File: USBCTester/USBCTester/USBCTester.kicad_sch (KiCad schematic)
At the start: 63 parts, among them J1 AUSB1-DFN-PTR3, J2 AUSB1-DFN-PTR3, J4 Conn_01x03, J5 Conn_01x08, J6 Conn_01x03, SW1 SW_Push, U1 74HC595, U2 74HC595, U3 74HC595, U4 74HC595, U5 74HC595, U6 74HC595, U7 RaspberryPi_Pico

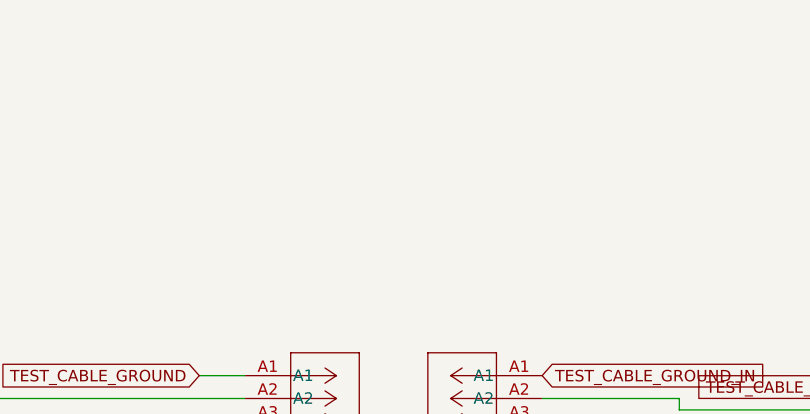
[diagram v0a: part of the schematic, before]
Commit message: add power plane and vias for high current and decoupling caps
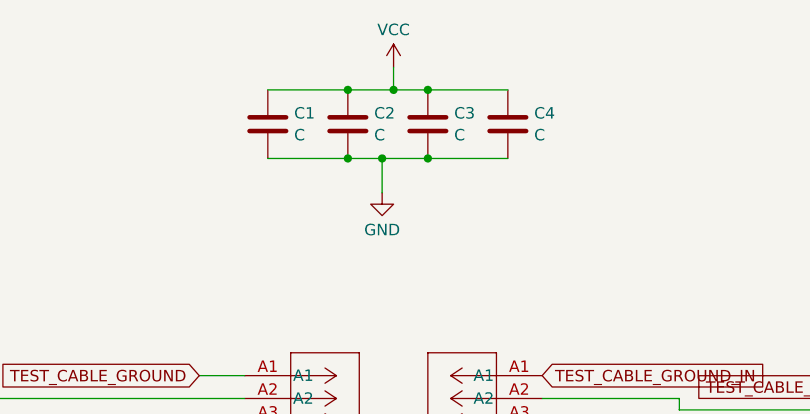
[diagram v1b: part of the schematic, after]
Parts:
- added C1, C2, C3, C4: C, symbol Device:C
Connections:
- net GND: now also C1.2, C2.2, C3.2, C4.2
- net VCC: now also C1.1, C2.1, C3.1, C4.1
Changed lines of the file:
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@@
   (junction (at 215.9 29.21) (diameter 0) (color 0 0 0 0)
   )
+  (junction (at 113.03 22.86) (diameter 0) (color 0 0 0 0)
+  )
   (junction (at 279.4 50.8) (diameter 0) (color 0 0 0 0)
   )
@@
   (junction (at 279.4 87.63) (diameter 0) (color 0 0 0 0)
   )
+  (junction (at 118.11 22.86) (diameter 0) (color 0 0 0 0)
+  )
+  (junction (at 113.03 30.48) (diameter 0) (color 0 0 0 0)
+  )
   (junction (at 220.98 142.24) (diameter 0) (color 0 0 0 0)
   )
@@
   (junction (at 279.4 134.62) (diameter 0) (color 0 0 0 0)
   )
+  (junction (at 116.84 30.48) (diameter 0) (color 0 0 0 0)
+  )
   (junction (at 101.6 123.19) (diameter 0) (color 0 0 0 0)
   )
@@
   (junction (at 229.87 100.33) (diameter 0) (color 0 0 0 0)
   )
+  (junction (at 121.92 22.86) (diameter 0) (color 0 0 0 0)
+  )
   (junction (at 279.4 142.24) (diameter 0) (color 0 0 0 0)
   )
@@
   (junction (at 279.4 48.26) (diameter 0) (color 0 0 0 0)
   )
+  (junction (at 121.92 30.48) (diameter 0) (color 0 0 0 0)
+  )
   (junction (at 279.4 139.7) (diameter 0) (color 0 0 0 0)
   )
@@
     (stroke (width 0) (type default))
   )
+  (wire (pts (xy 116.84 30.48) (xy 116.84 34.29))
+    (stroke (width 0) (type default))
+  )
   (wire (pts (xy 279.4 92.71) (xy 279.4 95.25))
     (stroke (width 0) (type default))
@@
     (stroke (width 0) (type default))
   )
+  (wire (pts (xy 121.92 30.48) (xy 130.81 30.48))
+    (stroke (width 0) (type default))
+  )
   (wire (pts (xy 50.8 120.65) (xy 50.8 130.81))
     (stroke (width 0) (type default))
@@
     (stroke (width 0) (type default))
   )
+  (wire (pts (xy 113.03 30.48) (xy 116.84 30.48))
+    (stroke (width 0) (type default))
+  )
   (wire (pts (xy 279.4 132.08) (xy 279.4 134.62))
     (stroke (width 0) (type default))
@@
     (stroke (width 0) (type default))
   )
+  (wire (pts (xy 113.03 22.86) (xy 118.11 22.86))
+    (stroke (width 0) (type default))
+  )
   (wire (pts (xy 176.53 72.39) (xy 176.53 71.12))
     (stroke (width 0) (type default))
@@
     (stroke (width 0) (type default))
   )
+  (wire (pts (xy 118.11 20.32) (xy 118.11 22.86))
+    (stroke (width 0) (type default))
+  )
   (wire (pts (xy 96.52 67.31) (xy 101.6 67.31))
     (stroke (width 0) (type default))
@@
     (stroke (width 0) (type default))
   )
+  (wire (pts (xy 104.14 22.86) (xy 113.03 22.86))
+    (stroke (width 0) (type default))
+  )
   (wire (pts (xy 279.4 97.79) (xy 279.4 100.33))
     (stroke (width 0) (type default))
@@
     (stroke (width 0) (type default))
   )
+  (wire (pts (xy 121.92 22.86) (xy 130.81 22.86))
+    (stroke (width 0) (type default))
+  )
   (wire (pts (xy 279.4 147.32) (xy 279.4 152.4))
     (stroke (width 0) (type default))
@@
     (stroke (width 0) (type default))
   )
+  (wire (pts (xy 104.14 30.48) (xy 113.03 30.48))
+    (stroke (width 0) (type default))
+  )
   (wire (pts (xy 259.08 97.79) (xy 264.16 97.79))
     (stroke (width 0) (type default))
@@
     (stroke (width 0) (type default))
   )
+  (wire (pts (xy 118.11 22.86) (xy 121.92 22.86))
+    (stroke (width 0) (type default))
+  )
   (wire (pts (xy 279.4 100.33) (xy 279.4 102.87))
     (stroke (width 0) (type default))
@@
     (stroke (width 0) (type default))
   )
+  (wire (pts (xy 116.84 30.48) (xy 121.92 30.48))
+    (stroke (width 0) (type default))
+  )
   (wire (pts (xy 238.76 118.11) (xy 238.76 129.54))
     (stroke (width 0) (type default))
@@
     )
   )
+  (symbol (lib_id "Device:C") (at 113.03 26.67 0) (unit 1)
+    (in_bom yes) (on_board yes) (dnp no) (fields_autoplaced)
+    (property "Reference" "C2" (at 115.951 25.4579 0)
+      (effects (font (size 1.27 1.27)) (justify left))
+    )
+    (property "Value" "C" (at 115.951 27.8821 0)
+      (effects (font (size 1.27 1.27)) (justify left))
+    )
+    (property "Footprint" "" (at 113.9952 30.48 0)
+      (effects (font (size 1.27 1.27)) hide)
+    )
+    (property "Datasheet" "~" (at 113.03 26.67 0)
+      (effects (font (size 1.27 1.27)) hide)
+    )
+    (pin "1")
+    (pin "2")
+    (instances
+      (project "USBCTester"
+        (path "/8a9ba22b-e32e-4058-9f6d-d23fc913e7b1"
+          (reference "C2") (unit 1)
+        )
+      )
+    )
+  )
   (symbol (lib_id "Device:R") (at 267.97 87.63 90) (unit 1)
     (in_bom yes) (on_board yes) (dnp no)
@@
     )
   )
+  (symbol (lib_id "power:VCC") (at 118.11 20.32 0) (unit 1)
+    (in_bom yes) (on_board yes) (dnp no) (fields_autoplaced)
+    (property "Reference" "#PWR015" (at 118.11 24.13 0)
+      (effects (font (size 1.27 1.27)) hide)
+    )
+    (property "Value" "VCC" (at 118.11 16.1869 0)
+      (effects (font (size 1.27 1.27)))
+    )
+    (property "Footprint" "" (at 118.11 20.32 0)
+      (effects (font (size 1.27 1.27)) hide)
+    )
+    (property "Datasheet" "" (at 118.11 20.32 0)
+      (effects (font (size 1.27 1.27)) hide)
+    )
+    (pin "1")
+    (instances
+      (project "USBCTester"
+        (path "/8a9ba22b-e32e-4058-9f6d-d23fc913e7b1"
+          (reference "#PWR015") (unit 1)
+        )
+      )
+    )
+  )
   (symbol (lib_id "Device:R") (at 267.97 139.7 90) (unit 1)
     (in_bom yes) (on_board yes) (dnp no)
@@
     )
   )
+  (symbol (lib_id "power:GND") (at 116.84 34.29 0) (unit 1)
+    (in_bom yes) (on_board yes) (dnp no) (fields_autoplaced)
+    (property "Reference" "#PWR017" (at 116.84 40.64 0)
+      (effects (font (size 1.27 1.27)) hide)
+    )
+    (property "Value" "GND" (at 116.84 38.4231 0)
+      (effects (font (size 1.27 1.27)))
+    )
+    (property "Footprint" "" (at 116.84 34.29 0)
+      (effects (font (size 1.27 1.27)) hide)
+    )
+    (property "Datasheet" "" (at 116.84 34.29 0)
+      (effects (font (size 1.27 1.27)) hide)
+    )
+    (pin "1")
+    (instances
+      (project "USBCTester"
+        (path "/8a9ba22b-e32e-4058-9f6d-d23fc913e7b1"
+          (reference "#PWR017") (unit 1)
+        )
+      )
+    )
+  )
   (symbol (lib_id "Device:R") (at 267.97 132.08 90) (unit 1)
     (in_bom yes) (on_board yes) (dnp no)
@@
     )
   )
+  (symbol (lib_id "Device:C") (at 130.81 26.67 0) (unit 1)
+    (in_bom yes) (on_board yes) (dnp no) (fields_autoplaced)
+    (property "Reference" "C4" (at 133.731 25.4579 0)
+      (effects (font (size 1.27 1.27)) (justify left))
+    )
+    (property "Value" "C" (at 133.731 27.8821 0)
+      (effects (font (size 1.27 1.27)) (justify left))
+    )
+    (property "Footprint" "" (at 131.7752 30.48 0)
+      (effects (font (size 1.27 1.27)) hide)
+    )
+    (property "Datasheet" "~" (at 130.81 26.67 0)
+      (effects (font (size 1.27 1.27)) hide)
+    )
+    (pin "1")
+    (pin "2")
+    (instances
+      (project "USBCTester"
+        (path "/8a9ba22b-e32e-4058-9f6d-d23fc913e7b1"
+          (reference "C4") (unit 1)
+        )
+      )
+    )
+  )
   (symbol (lib_id "power:+3V3") (at 190.5 25.4 270) (unit 1)
     (in_bom yes) (on_board yes) (dnp no) (fields_autoplaced)
@@
     )
   )
+  (symbol (lib_id "Device:C") (at 121.92 26.67 0) (unit 1)
+    (in_bom yes) (on_board yes) (dnp no) (fields_autoplaced)
+    (property "Reference" "C3" (at 124.841 25.4579 0)
+      (effects (font (size 1.27 1.27)) (justify left))
+    )
+    (property "Value" "C" (at 124.841 27.8821 0)
+      (effects (font (size 1.27 1.27)) (justify left))
+    )
+    (property "Footprint" "" (at 122.8852 30.48 0)
+      (effects (font (size 1.27 1.27)) hide)
+    )
+    (property "Datasheet" "~" (at 121.92 26.67 0)
+      (effects (font (size 1.27 1.27)) hide)
+    )
+    (pin "1")
+    (pin "2")
+    (instances
+      (project "USBCTester"
+        (path "/8a9ba22b-e32e-4058-9f6d-d23fc913e7b1"
+          (reference "C3") (unit 1)
+        )
+      )
+    )
+  )
   (symbol (lib_id "Device:R") (at 267.97 50.8 90) (unit 1)
     (in_bom yes) (on_board yes) (dnp no)
@@
         )
       )
+    )
+  )
+  (symbol (lib_id "Device:C") (at 104.14 26.67 0) (unit 1)
+    (in_bom yes) (on_board yes) (dnp no) (fields_autoplaced)
+    (property "Reference" "C1" (at 107.061 25.4579 0)
+      (effects (font (size 1.27 1.27)) (justify left))
+    )
+    (property "Value" "C" (at 107.061 27.8821 0)
+      (effects (font (size 1.27 1.27)) (justify left))
+    )
+    (property "Footprint" "" (at 105.1052 30.48 0)
+      (effects (font (size 1.27 1.27)) hide)
+    )
+    (property "Datasheet" "~" (at 104.14 26.67 0)
+      (effects (font (size 1.27 1.27)) hide)
+    )
+    (pin "1")
+    (pin "2")
+    (instances
+      (project "USBCTester"
+        (path "/8a9ba22b-e32e-4058-9f6d-d23fc913e7b1"
+          (reference "C1") (unit 1)
+        )
+      )

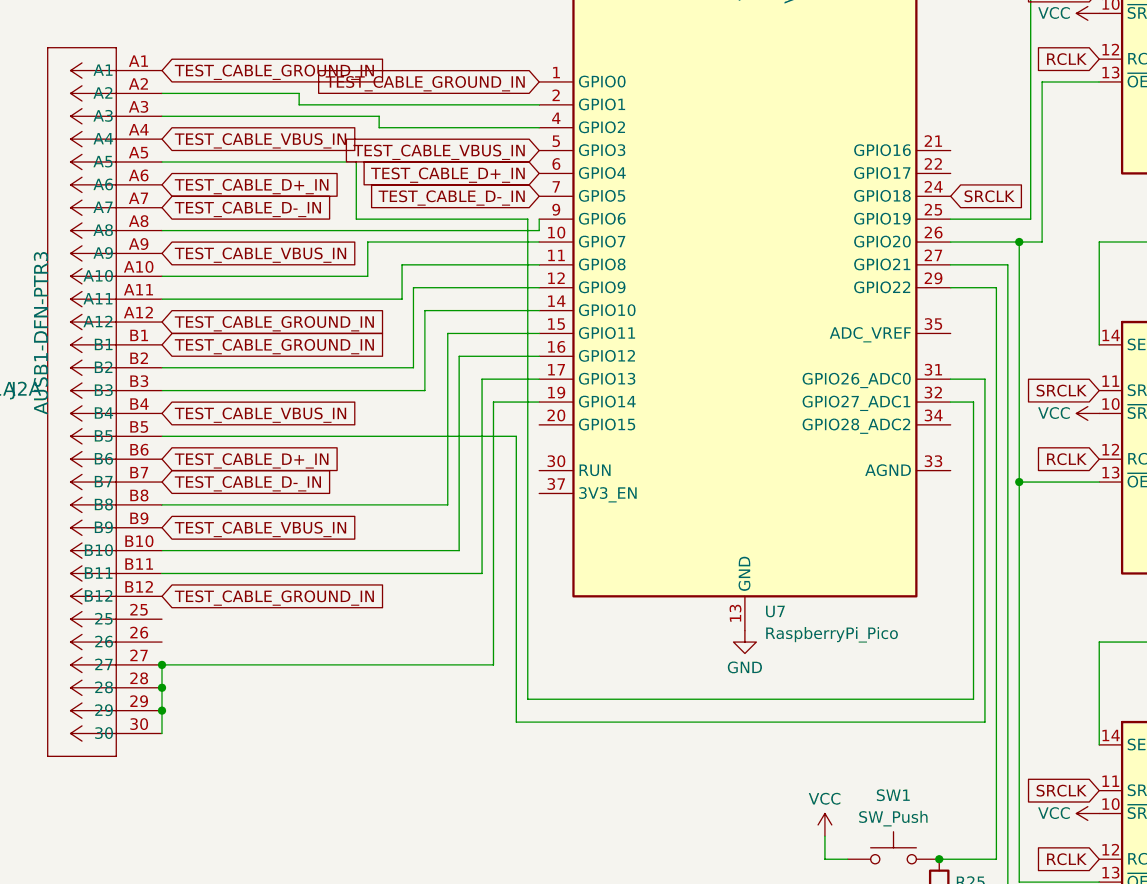
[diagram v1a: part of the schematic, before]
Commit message: continu wiring and add decoupling caps
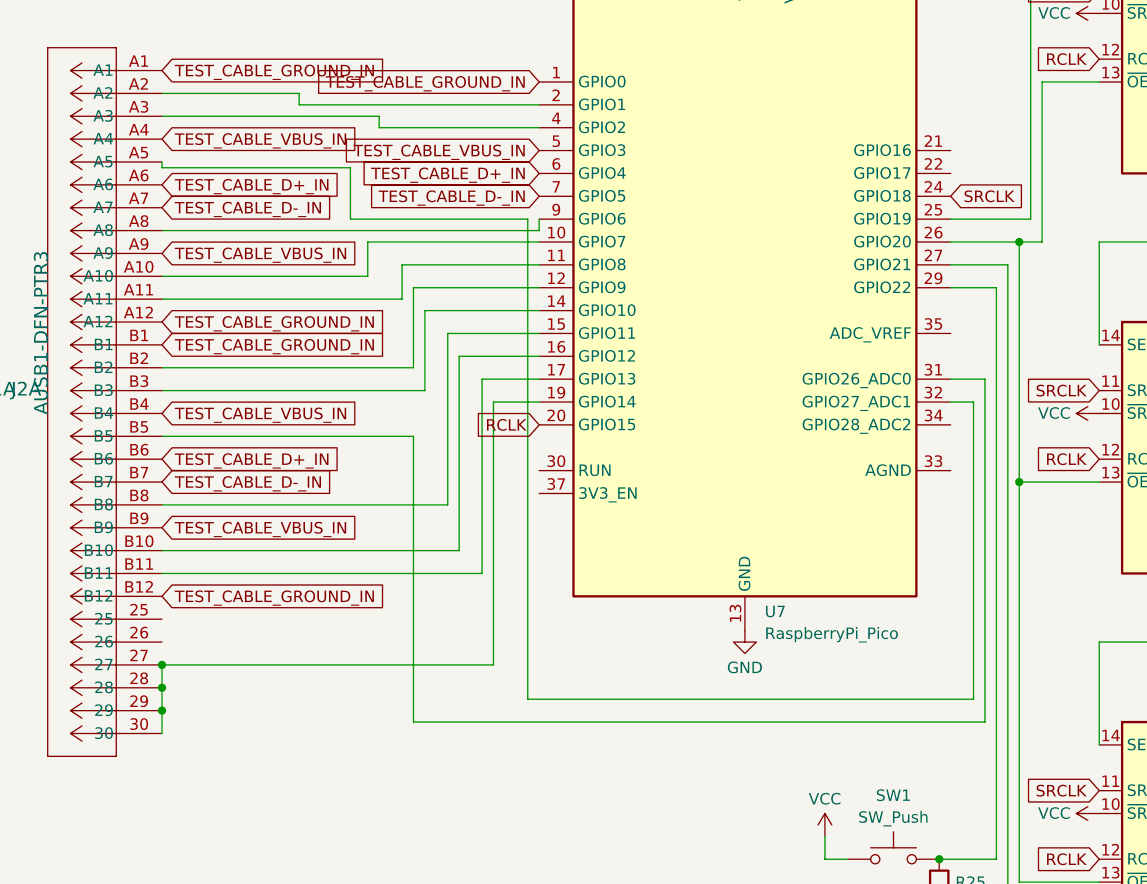
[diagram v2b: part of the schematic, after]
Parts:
- C1, C2, C3, C4: footprint (none) -> Capacitor_SMD:C_0603_1608Metric
- SW1: footprint (none) -> Button_Switch_SMD:SW_Push_1P1T_NO_6x6mm_H9.5mm
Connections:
- net RCLK: now also U7.20 (GPIO15)
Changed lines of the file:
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@@
     (stroke (width 0) (type default))
   )
+  (wire (pts (xy 134.62 65.4073) (xy 134.62 64.77))
+    (stroke (width 0) (type default))
+  )
   (wire (pts (xy 232.41 73.66) (xy 232.41 55.88))
     (stroke (width 0) (type default))
@@
     (stroke (width 0) (type default))
   )
-  (wire (pts (xy 173.99 95.25) (xy 173.99 127))
+  (wire (pts (xy 162.56 95.25) (xy 162.56 127))
     (stroke (width 0) (type default))
   )
@@
     (stroke (width 0) (type default))
   )
-  (wire (pts (xy 156.21 71.12) (xy 156.21 64.77))
+  (wire (pts (xy 155.5565 71.12) (xy 155.5565 65.4073))
     (stroke (width 0) (type default))
   )
@@
     (stroke (width 0) (type default))
   )
-  (wire (pts (xy 156.21 71.12) (xy 175.26 71.12))
+  (wire (pts (xy 155.5565 71.12) (xy 175.26 71.12))
     (stroke (width 0) (type default))
   )
@@
     (stroke (width 0) (type default))
   )
+  (wire (pts (xy 134.62 65.4073) (xy 155.5565 65.4073))
+    (stroke (width 0) (type default))
+  )
   (wire (pts (xy 259.08 73.66) (xy 238.76 73.66))
     (stroke (width 0) (type default))
@@
     (stroke (width 0) (type default))
   )
-  (wire (pts (xy 134.62 95.25) (xy 173.99 95.25))
+  (wire (pts (xy 134.62 95.25) (xy 162.56 95.25))
     (stroke (width 0) (type default))
   )
@@
     (stroke (width 0) (type default))
   )
-  (wire (pts (xy 156.21 64.77) (xy 134.62 64.77))
-    (stroke (width 0) (type default))
-  )
   (wire (pts (xy 134.62 125.73) (xy 134.62 128.27))
     (stroke (width 0) (type default))
@@
     (stroke (width 0) (type default))
   )
-  (wire (pts (xy 173.99 127) (xy 226.06 127))
+  (wire (pts (xy 162.56 127) (xy 226.06 127))
     (stroke (width 0) (type default))
   )
@@
     )
   )
+  (global_label "RCLK" (shape input) (at 176.53 93.98 180) (fields_autoplaced)
+    (effects (font (size 1.27 1.27)) (justify right))
+    (property "Intersheetrefs" "${INTERSHEET_REFS}" (at 168.7067 93.98 0)
+      (effects (font (size 1.27 1.27)) (justify right) hide)
+    )
+  )
   (global_label "TEST_CABLE_D-" (shape input) (at 50.8 69.85 0) (fields_autoplaced)
     (effects (font (size 1.27 1.27)) (justify left))
@@
       (effects (font (size 1.27 1.27)) (justify left))
     )
-    (property "Footprint" "" (at 113.9952 30.48 0)
+    (property "Footprint" "Capacitor_SMD:C_0603_1608Metric" (at 113.9952 30.48 0)
       (effects (font (size 1.27 1.27)) hide)
     )
@@
       (effects (font (size 1.27 1.27)))
     )
-    (property "Footprint" "" (at 215.9 137.16 0)
+    (property "Footprint" "Button_Switch_SMD:SW_Push_1P1T_NO_6x6mm_H9.5mm" (at 215.9 137.16 0)
       (effects (font (size 1.27 1.27)) hide)
     )
@@
       (effects (font (size 1.27 1.27)) (justify left))
     )
-    (property "Footprint" "" (at 131.7752 30.48 0)
+    (property "Footprint" "Capacitor_SMD:C_0603_1608Metric" (at 131.7752 30.48 0)
       (effects (font (size 1.27 1.27)) hide)
     )
@@
       (effects (font (size 1.27 1.27)) (justify left))
     )
-    (property "Footprint" "" (at 122.8852 30.48 0)
+    (property "Footprint" "Capacitor_SMD:C_0603_1608Metric" (at 122.8852 30.48 0)
       (effects (font (size 1.27 1.27)) hide)
     )
@@
       (effects (font (size 1.27 1.27)) (justify left))
     )
-    (property "Footprint" "" (at 105.1052 30.48 0)
+    (property "Footprint" "Capacitor_SMD:C_0603_1608Metric" (at 105.1052 30.48 0)
       (effects (font (size 1.27 1.27)) hide)
     )
